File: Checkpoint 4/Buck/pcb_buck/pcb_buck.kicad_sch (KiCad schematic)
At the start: 18 parts, among them J2 Conn_01x04_Socket, M1 IRF530, M2 IRF530, U1 IR2104

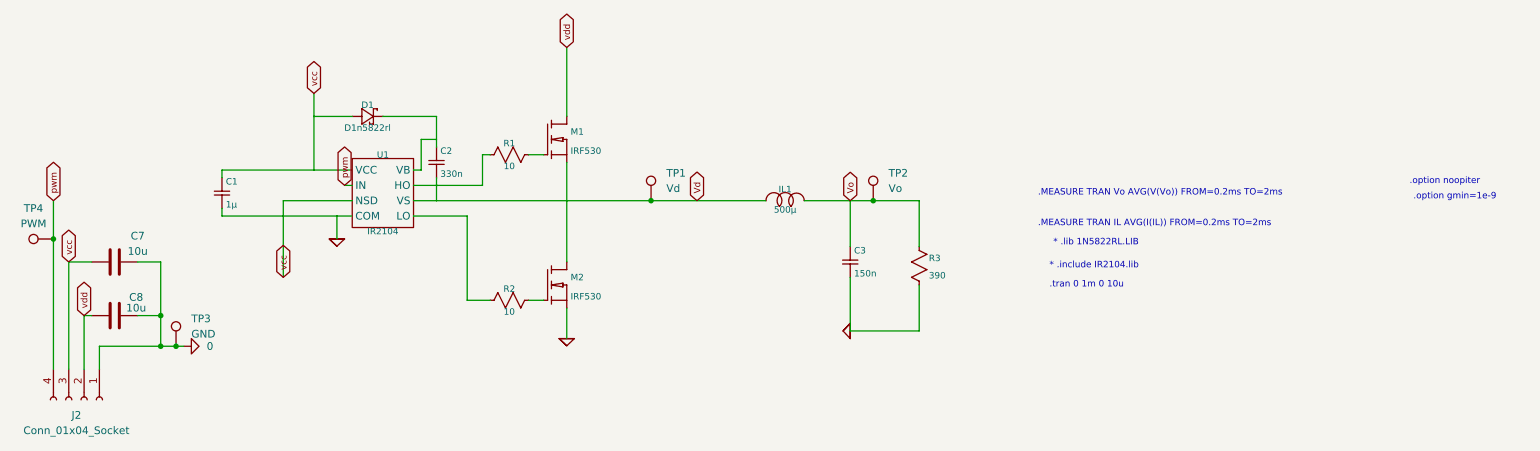
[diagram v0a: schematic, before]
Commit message: sube buck a lazo cerrado
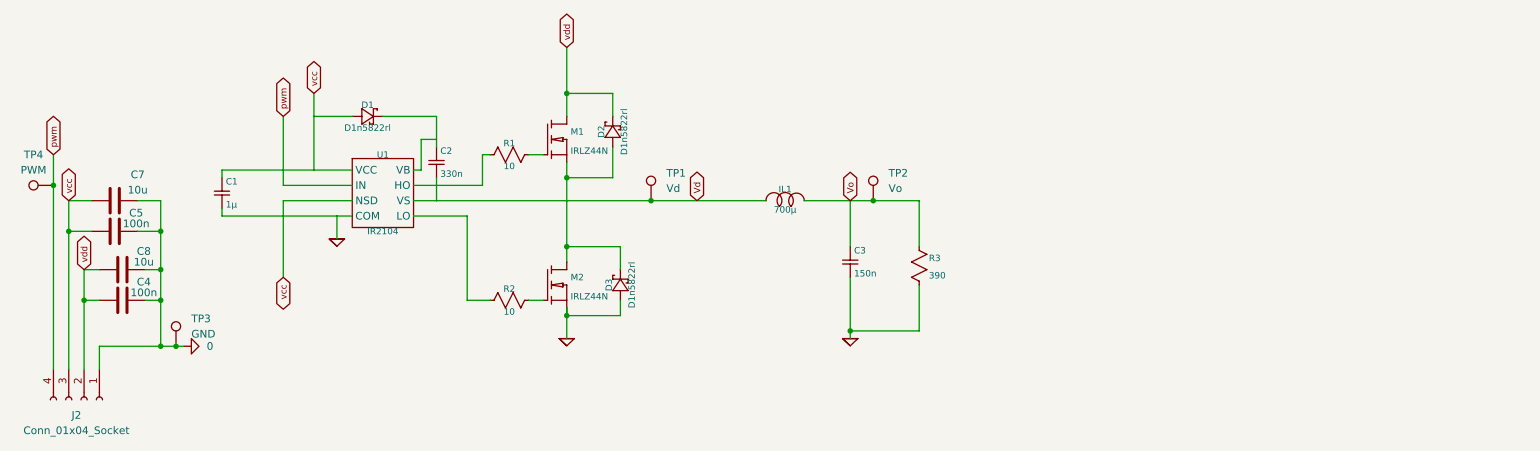
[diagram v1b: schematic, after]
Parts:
- added C4, C5: 100n, Capacitor_THT:C_Disc_D3.4mm_W2.1mm_P2.50mm, symbol Device:C
- added D2, D3: D1n5822rl, Diode_THT:D_DO-27_P12.70mm_Horizontal, symbol ltspice:schottky
- IL1: value 500µ -> 700µ
- M1, M2: value IRF530 -> IRLZ44N
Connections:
- net 0: now also C4.2, C5.2, D3.1 (+)
- net Vd: now also D2.1 (+), D3.2 (-)
- net vcc: now also C5.1
- net vdd: now also C4.1, D2.2 (-)
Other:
- note removed: "* .include IR2104.lib"
- note removed: "* .lib 1N5822RL.LIB"
- note removed: ".MEASURE TRAN IL AVG(I(IL)) FROM=0.2ms TO=2ms"
- note removed: ".MEASURE TRAN Vo AVG(V(Vo)) FROM=0.2ms TO=2ms"
- note removed: ".option gmin=1e-9"
- note removed: ".option noopiter"
- note removed: ".tran 0 1m 0 10u"
- moved on the sheet: C7, C8, TP4

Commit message: PCB Buck new
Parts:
- C8: value 10u -> 470u
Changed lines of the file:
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@@
 			)
 		)
-		(property "Value" "10u"
+		(property "Value" "470u"
 			(at 55.626 116.84 90)
 			(effects

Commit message: a ver si ahora si funcan los pcb sino me mato
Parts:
- added TP5: GND, TestPoint:TestPoint_THTPad_2.0x2.0mm_Drill1.0mm, symbol Connector:TestPoint
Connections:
- net 0: now also TP5.1
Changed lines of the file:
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@@
+	)
+	(junction
+		(at 175.26 128.27)
+		(diameter 0)
+		(color 0 0 0 0)
 	)
 	(junction
@@
 	(wire
 		(pts
-			(xy 184.15 128.27) (xy 172.72 128.27)
+			(xy 184.15 128.27) (xy 175.26 128.27)
+		)
+		(stroke
+			(width 0.1524)
+			(type solid)
+		)
+	)
+	(wire
+		(pts
+			(xy 175.26 128.27) (xy 172.72 128.27)
 		)
 		(stroke
@@
 					(unit 1)
 				)
+			)
+		)
+	)
+	(symbol
+		(lib_id "Connector:TestPoint")
+		(at 175.26 128.27 0)
+		(unit 1)
+		(exclude_from_sim no)
+		(in_bom yes)
+		(on_board yes)
+		(dnp no)
+		(fields_autoplaced yes)
+		(property "Reference" "TP5"
+			(at 177.8 123.6979 0)
+			(effects
+				(font
+					(size 1.27 1.27)
+				)
+				(justify left)
+			)
+		)
+		(property "Value" "GND"
+			(at 177.8 126.2379 0)
+			(effects
+				(font
+					(size 1.27 1.27)
+				)
+				(justify left)
+			)
+		)
+		(property "Footprint" "TestPoint:TestPoint_THTPad_2.0x2.0mm_Drill1.0mm"
+			(at 180.34 128.27 0)
+			(effects
+				(font
+					(size 1.27 1.27)
+				)
+				(hide yes)
+			)
+		)
+		(property "Datasheet" "~"
+			(at 180.34 128.27 0)
+			(effects
+				(font
+					(size 1.27 1.27)
+				)
+				(hide yes)
+			)
+		)
+		(property "Description" "test point"
+			(at 175.26 128.27 0)
+			(effects
+				(font
+					(size 1.27 1.27)
+				)
+				(hide yes)
+			)
+		)
+		(pin "1"
+		)
+		(instances
+			(project "pcb_buck"
+				(path "/c07dc6f8-4993-4f99-9fe5-e6b8a0415b6f"
+					(reference "TP5")
+					(unit 1)
+				)
